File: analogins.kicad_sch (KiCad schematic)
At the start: 13 parts, among them J11 Conn_01x04_Socket, U12 MCP6042

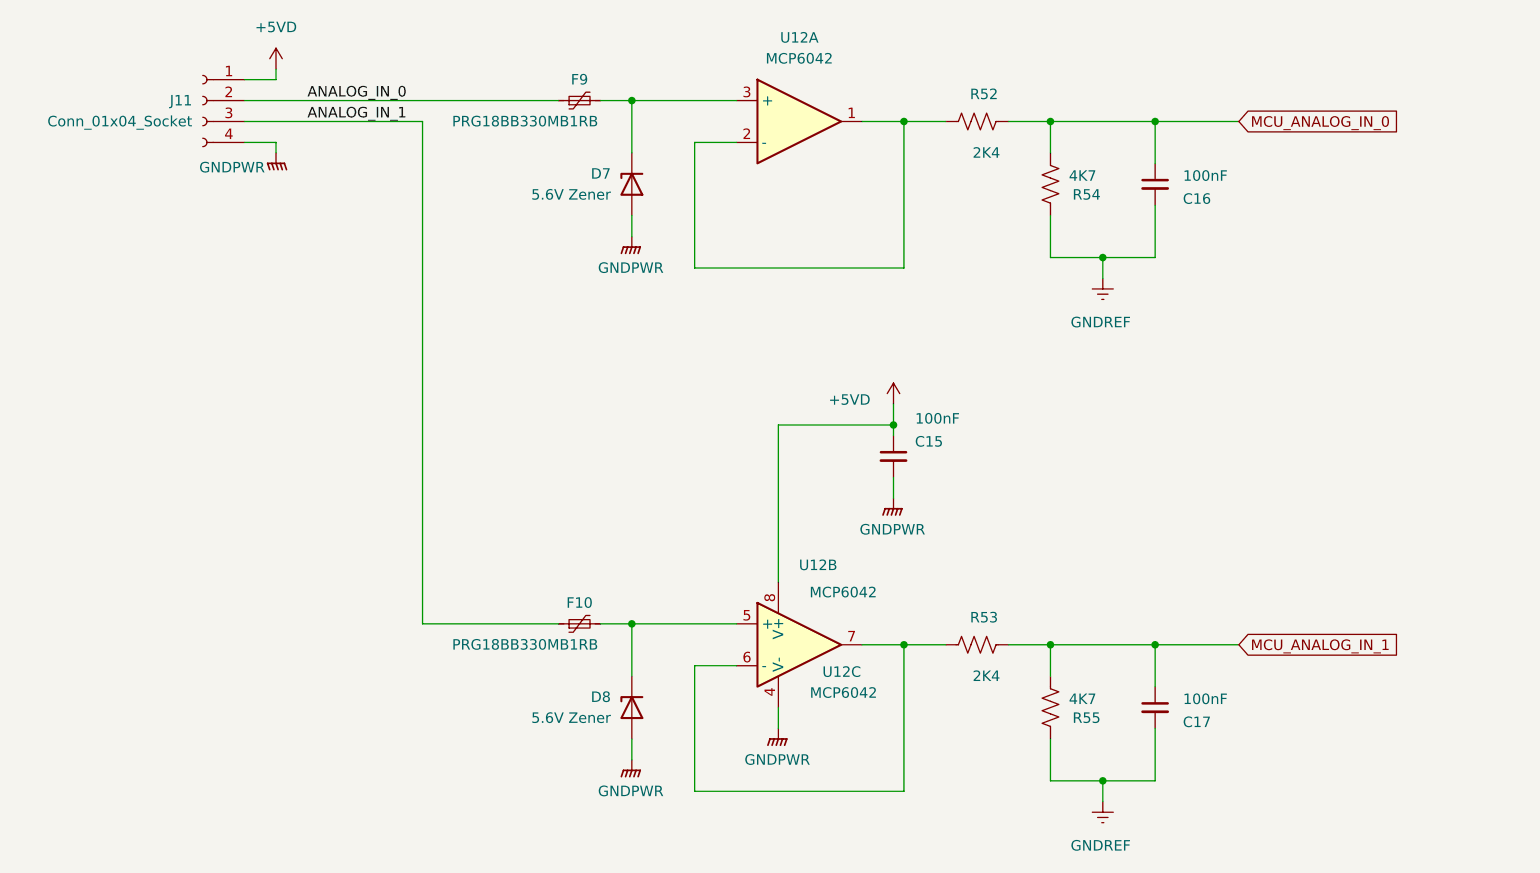
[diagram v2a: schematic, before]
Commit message: Added 3d Models for new terminal connectors for easy board verification before committing to build
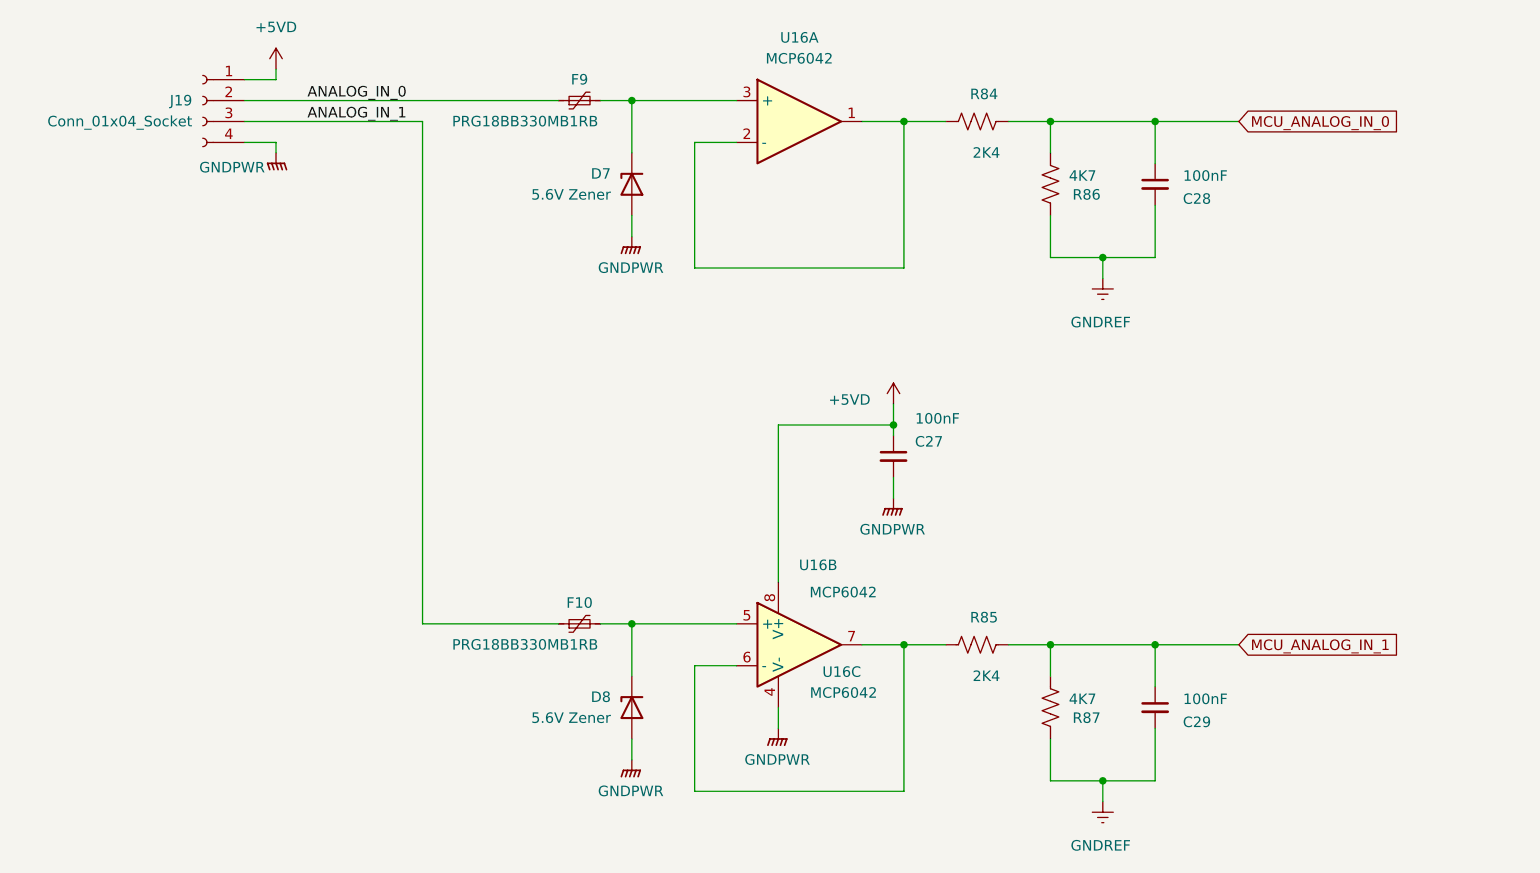
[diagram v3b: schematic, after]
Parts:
- renumbered C15 to C27, C16 to C28, C17 to C29, J11 to J19, R52 to R84, R53 to R85, R54 to R86, R55 to R87, U12 to U16
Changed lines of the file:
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@@
 		(on_board yes)
 		(dnp no)
-		(property "Reference" "#PWR0135"
+		(property "Reference" "#PWR0203"
 			(at 151.13 86.36 0)
 			(effects
@@
 			(project "Remora Nucleo F446ZE Hat"
 				(path "/5473abc6-7b93-43cc-a401-f691c4d7d7cf/c4dfed52-cba5-44a6-a641-6a90c0b6c0aa"
-					(reference "#PWR0135")
+					(reference "#PWR0203")
 					(unit 1)
 				)
@@
 		(on_board yes)
 		(dnp no)
-		(property "Reference" "R52"
+		(property "Reference" "R84"
 			(at 163.83 44.958 90)
 			(effects
@@
 			(project "Remora Nucleo F446ZE Hat"
 				(path "/5473abc6-7b93-43cc-a401-f691c4d7d7cf/c4dfed52-cba5-44a6-a641-6a90c0b6c0aa"
-					(reference "R52")
+					(reference "R84")
 					(unit 1)
 				)
@@
 		(on_board yes)
 		(dnp no)
-		(property "Reference" "U12"
+		(property "Reference" "U16"
 			(at 142.494 115.062 0)
 			(effects
@@
 			(project ""
 				(path "/5473abc6-7b93-43cc-a401-f691c4d7d7cf/c4dfed52-cba5-44a6-a641-6a90c0b6c0aa"
-					(reference "U12")
+					(reference "U16")
 					(unit 3)
 				)
@@
 		(on_board yes)
 		(dnp no)
-		(property "Reference" "C15"
+		(property "Reference" "C27"
 			(at 155.448 87.122 0)
 			(effects
@@
 			(project "Remora Nucleo F446ZE Hat"
 				(path "/5473abc6-7b93-43cc-a401-f691c4d7d7cf/c4dfed52-cba5-44a6-a641-6a90c0b6c0aa"
-					(reference "C15")
+					(reference "C27")
 					(unit 1)
 				)
@@
 		(on_board yes)
 		(dnp no)
-		(property "Reference" "R55"
+		(property "Reference" "R87"
 			(at 176.276 120.65 0)
 			(effects
@@
 			(project "Remora Nucleo F446ZE Hat"
 				(path "/5473abc6-7b93-43cc-a401-f691c4d7d7cf/c4dfed52-cba5-44a6-a641-6a90c0b6c0aa"
-					(reference "R55")
+					(reference "R87")
 					(unit 1)
 				)
@@
 		(dnp no)
 		(fields_autoplaced yes)
-		(property "Reference" "#PWR0132"
+		(property "Reference" "#PWR0200"
 			(at 119.38 67.31 0)
 			(effects
@@
 			(project "Remora Nucleo F446ZE Hat"
 				(path "/5473abc6-7b93-43cc-a401-f691c4d7d7cf/c4dfed52-cba5-44a6-a641-6a90c0b6c0aa"
-					(reference "#PWR0132")
+					(reference "#PWR0200")
 					(unit 1)
 				)
@@
 		(dnp no)
 		(fields_autoplaced yes)
-		(property "Reference" "#PWR0133"
+		(property "Reference" "#PWR0201"
 			(at 119.38 130.81 0)
 			(effects
@@
 			(project "Remora Nucleo F446ZE Hat"
 				(path "/5473abc6-7b93-43cc-a401-f691c4d7d7cf/c4dfed52-cba5-44a6-a641-6a90c0b6c0aa"
-					(reference "#PWR0133")
+					(reference "#PWR0201")
 					(unit 1)
 				)
@@
 		(dnp no)
 		(fields_autoplaced yes)
-		(property "Reference" "#PWR0134"
+		(property "Reference" "#PWR0202"
 			(at 137.16 127 0)
 			(effects
@@
 			(project "Remora Nucleo F446ZE Hat"
 				(path "/5473abc6-7b93-43cc-a401-f691c4d7d7cf/c4dfed52-cba5-44a6-a641-6a90c0b6c0aa"
-					(reference "#PWR0134")
+					(reference "#PWR0202")
 					(unit 1)
 				)
@@
 		(on_board yes)
 		(dnp no)
-		(property "Reference" "C16"
+		(property "Reference" "C28"
 			(at 187.96 57.658 0)
 			(effects
@@
 			(project "Remora Nucleo F446ZE Hat"
 				(path "/5473abc6-7b93-43cc-a401-f691c4d7d7cf/c4dfed52-cba5-44a6-a641-6a90c0b6c0aa"
-					(reference "C16")
+					(reference "C28")
 					(unit 1)
 				)
@@
 		(on_board yes)
 		(dnp no)
-		(property "Reference" "U12"
+		(property "Reference" "U16"
 			(at 141.986 102.108 0)
 			(effects
@@
 			(project ""
 				(path "/5473abc6-7b93-43cc-a401-f691c4d7d7cf/c4dfed52-cba5-44a6-a641-6a90c0b6c0aa"
-					(reference "U12")
+					(reference "U16")
 					(unit 2)
 				)
@@
 		(dnp no)
 		(fields_autoplaced yes)
-		(property "Reference" "J11"
+		(property "Reference" "J19"
 			(at 66.04 45.7199 0)
 			(effects
@@
 			(project "Remora Nucleo F446ZE Hat"
 				(path "/5473abc6-7b93-43cc-a401-f691c4d7d7cf/c4dfed52-cba5-44a6-a641-6a90c0b6c0aa"
-					(reference "J11")
+					(reference "J19")
 					(unit 1)
 				)
@@
 		(dnp no)
 		(fields_autoplaced yes)
-		(property "Reference" "U12"
+		(property "Reference" "U16"
 			(at 139.7 38.1 0)
 			(effects
@@
 			(project ""
 				(path "/5473abc6-7b93-43cc-a401-f691c4d7d7cf/c4dfed52-cba5-44a6-a641-6a90c0b6c0aa"
-					(reference "U12")
+					(reference "U16")
 					(unit 1)
 				)
@@
 		(on_board yes)
 		(dnp no)
-		(property "Reference" "C17"
+		(property "Reference" "C29"
 			(at 187.96 121.158 0)
 			(effects
@@
 			(project "Remora Nucleo F446ZE Hat"
 				(path "/5473abc6-7b93-43cc-a401-f691c4d7d7cf/c4dfed52-cba5-44a6-a641-6a90c0b6c0aa"
-					(reference "C17")
+					(reference "C29")
 					(unit 1)
 				)
@@
 		(on_board no)
 		(dnp no)
-		(property "Reference" "#PWR0138"
+		(property "Reference" "#PWR0206"
 			(at 176.53 137.16 0)
 			(effects
@@
 			(project "Remora Nucleo F446ZE Hat"
 				(path "/5473abc6-7b93-43cc-a401-f691c4d7d7cf/c4dfed52-cba5-44a6-a641-6a90c0b6c0aa"
-					(reference "#PWR0138")
+					(reference "#PWR0206")
 					(unit 1)
 				)
@@
 		(dnp no)
 		(fields_autoplaced yes)
-		(property "Reference" "#PWR0136"
+		(property "Reference" "#PWR0204"
 			(at 151.13 99.06 0)
 			(effects
@@
 			(project "Remora Nucleo F446ZE Hat"
 				(path "/5473abc6-7b93-43cc-a401-f691c4d7d7cf/c4dfed52-cba5-44a6-a641-6a90c0b6c0aa"
-					(reference "#PWR0136")
+					(reference "#PWR0204")
 					(unit 1)
 				)
@@
 		(on_board yes)
 		(dnp no)
-		(property "Reference" "R54"
+		(property "Reference" "R86"
 			(at 176.276 57.15 0)
 			(effects
@@
 			(project "Remora Nucleo F446ZE Hat"
 				(path "/5473abc6-7b93-43cc-a401-f691c4d7d7cf/c4dfed52-cba5-44a6-a641-6a90c0b6c0aa"
-					(reference "R54")
+					(reference "R86")
 					(unit 1)
 				)
@@
 		(dnp no)
 		(fields_autoplaced yes)
-		(property "Reference" "#PWR0130"
+		(property "Reference" "#PWR0198"
 			(at 76.2 45.72 0)
 			(effects
@@
 			(project "Remora Nucleo F446ZE Hat"
 				(path "/5473abc6-7b93-43cc-a401-f691c4d7d7cf/c4dfed52-cba5-44a6-a641-6a90c0b6c0aa"
-					(reference "#PWR0130")
+					(reference "#PWR0198")
 					(unit 1)
 				)
@@
 		(on_board no)
 		(dnp no)
-		(property "Reference" "#PWR0137"
+		(property "Reference" "#PWR0205"
 			(at 176.53 73.66 0)
 			(effects
@@
 			(project "Remora Nucleo F446ZE Hat"
 				(path "/5473abc6-7b93-43cc-a401-f691c4d7d7cf/c4dfed52-cba5-44a6-a641-6a90c0b6c0aa"
-					(reference "#PWR0137")
+					(reference "#PWR0205")
 					(unit 1)
 				)
@@
 		(on_board no)
 		(dnp no)
-		(property "Reference" "#PWR0131"
+		(property "Reference" "#PWR0199"
 			(at 76.2 57.15 0)
 			(effects
@@
 			(project "Remora Nucleo F446ZE Hat"
 				(path "/5473abc6-7b93-43cc-a401-f691c4d7d7cf/c4dfed52-cba5-44a6-a641-6a90c0b6c0aa"
-					(reference "#PWR0131")
+					(reference "#PWR0199")
 					(unit 1)
 				)
@@
 		(on_board yes)
 		(dnp no)
-		(property "Reference" "R53"
+		(property "Reference" "R85"
 			(at 163.83 108.458 90)
 			(effects
@@
 			(project "Remora Nucleo F446ZE Hat"
 				(path "/5473abc6-7b93-43cc-a401-f691c4d7d7cf/c4dfed52-cba5-44a6-a641-6a90c0b6c0aa"
-					(reference "R53")
-					(unit 1)
-				)
+					(reference "R85")
+					(unit 1)
+				)

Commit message: Caught some errors with spacing of jumpers, did some BOM consolidation and included BOM. Updates to Gerbers to reflect new changes.
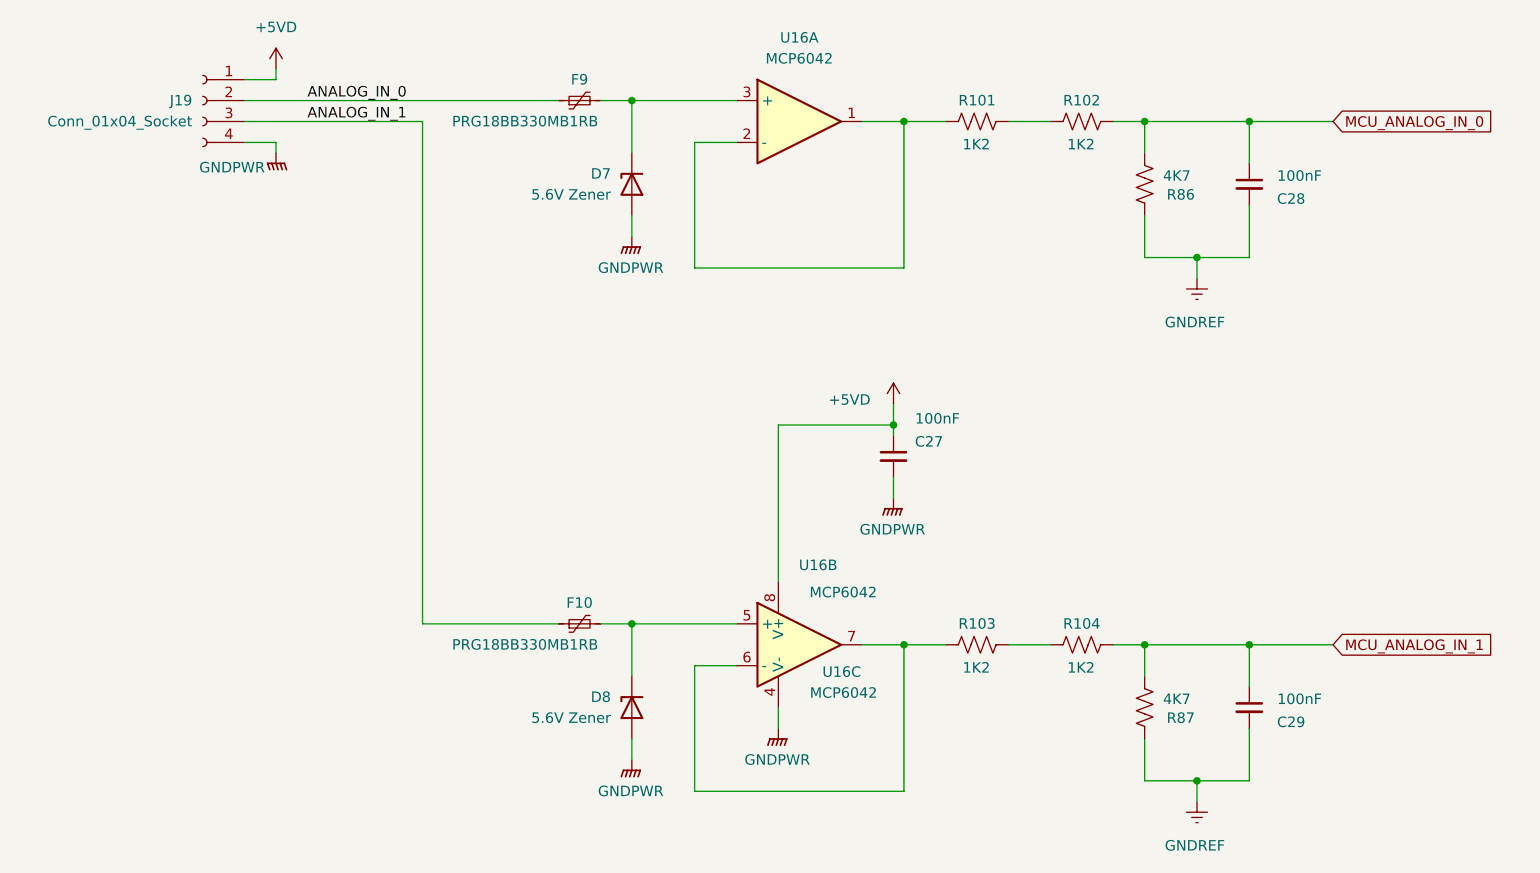
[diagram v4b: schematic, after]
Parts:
- removed R84, R85: 2K4, Resistor_SMD:R_1206_3216Metric_Pad1.30x1.75mm_HandSolder, symbol Device:R_US
- added R101, R102, R103, R104: 1K2, Resistor_SMD:R_1206_3216Metric_Pad1.30x1.75mm_HandSolder, symbol Device:R_US
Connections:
- net MCU_ANALOG_IN_0: now also R102.1
- net MCU_ANALOG_IN_1: now also R104.1
- net at U16.1, U16.2 (-): now also R101.2
- net at U16.6 (-), U16.7: now also R103.2
- new net: R101.1, R102.2
- new net: R103.1, R104.2
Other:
- moved on the sheet: C28, C29, R86, R87

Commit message: Some file changes and output new gerbers + BOM and centroid file for PCBWay Order
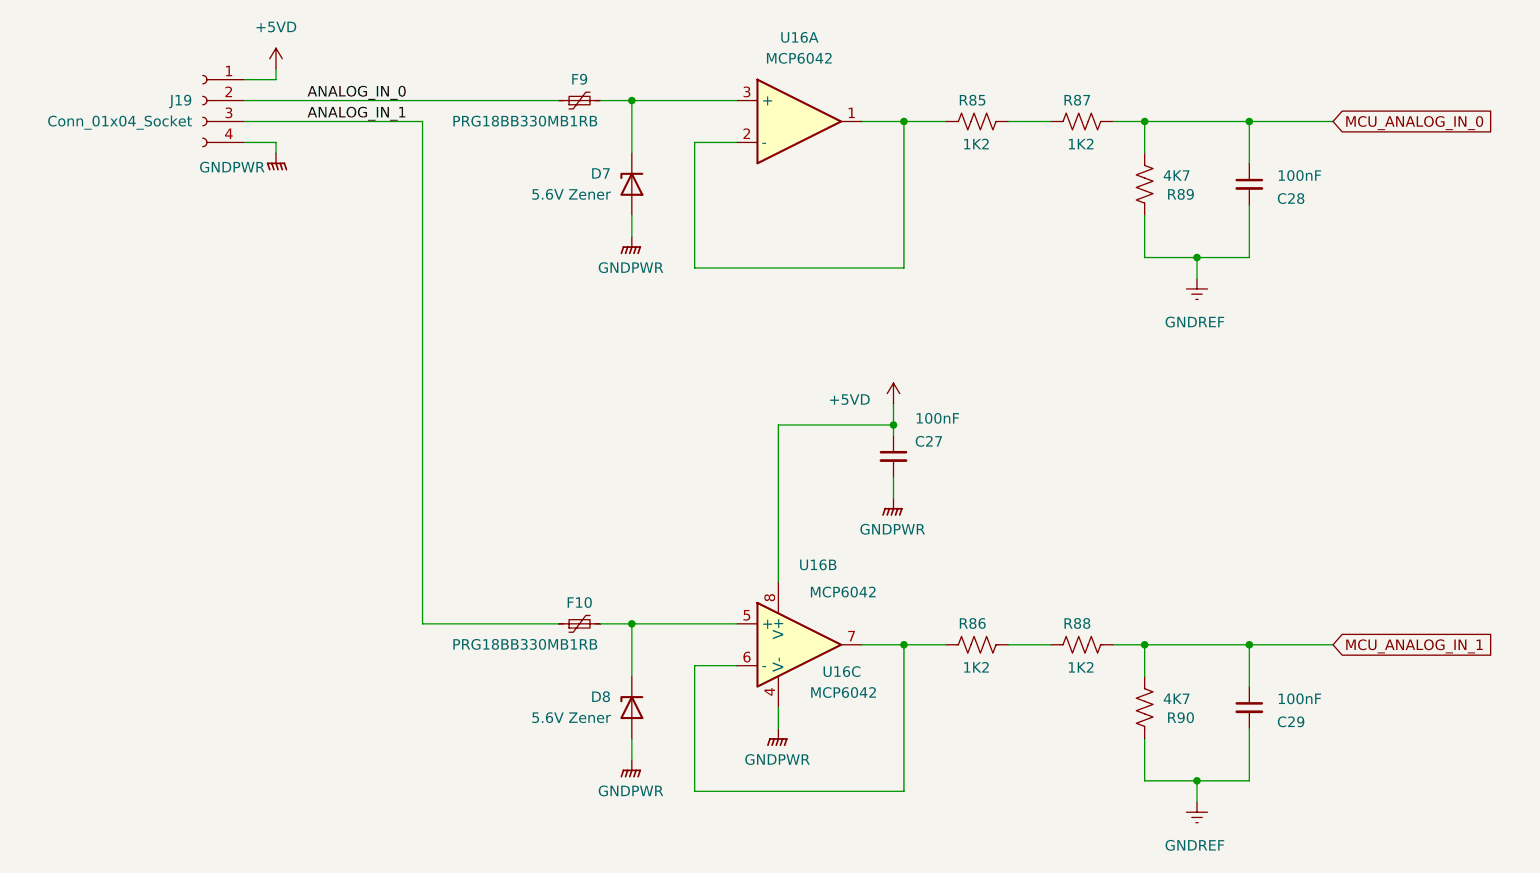
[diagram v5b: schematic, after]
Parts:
- renumbered R101 to R85, R103 to R86, R102 to R87, R104 to R88, R86 to R89, R87 to R90
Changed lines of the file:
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@@
 		(on_board yes)
 		(dnp no)
-		(property "Reference" "R101"
+		(property "Reference" "R85"
 			(at 159.004 45.72 90)
 			(effects
@@
 			(project "Remora Nucleo F446ZE Hat"
 				(path "/5473abc6-7b93-43cc-a401-f691c4d7d7cf/c4dfed52-cba5-44a6-a641-6a90c0b6c0aa"
-					(reference "R101")
+					(reference "R85")
 					(unit 1)
 				)
@@
 		(on_board yes)
 		(dnp no)
-		(property "Reference" "R102"
+		(property "Reference" "R87"
 			(at 171.704 45.72 90)
 			(effects
@@
 			(project "Remora Nucleo F446ZE Hat"
 				(path "/5473abc6-7b93-43cc-a401-f691c4d7d7cf/c4dfed52-cba5-44a6-a641-6a90c0b6c0aa"
-					(reference "R102")
+					(reference "R87")
 					(unit 1)
 				)
@@
 		(on_board yes)
 		(dnp no)
-		(property "Reference" "R87"
+		(property "Reference" "R90"
 			(at 187.706 120.65 0)
 			(effects
@@
 			(project "Remora Nucleo F446ZE Hat"
 				(path "/5473abc6-7b93-43cc-a401-f691c4d7d7cf/c4dfed52-cba5-44a6-a641-6a90c0b6c0aa"
-					(reference "R87")
+					(reference "R90")
 					(unit 1)
 				)
@@
 		(on_board yes)
 		(dnp no)
-		(property "Reference" "R103"
+		(property "Reference" "R86"
 			(at 159.004 109.22 90)
 			(effects
@@
 			(project "Remora Nucleo F446ZE Hat"
 				(path "/5473abc6-7b93-43cc-a401-f691c4d7d7cf/c4dfed52-cba5-44a6-a641-6a90c0b6c0aa"
-					(reference "R103")
+					(reference "R86")
 					(unit 1)
 				)
@@
 		(on_board yes)
 		(dnp no)
-		(property "Reference" "R104"
+		(property "Reference" "R88"
 			(at 171.704 109.22 90)
 			(effects
@@
 			(project "Remora Nucleo F446ZE Hat"
 				(path "/5473abc6-7b93-43cc-a401-f691c4d7d7cf/c4dfed52-cba5-44a6-a641-6a90c0b6c0aa"
-					(reference "R104")
+					(reference "R88")
 					(unit 1)
 				)
@@
 		(on_board yes)
 		(dnp no)
-		(property "Reference" "R86"
+		(property "Reference" "R89"
 			(at 187.706 57.15 0)
 			(effects
@@
 			(project "Remora Nucleo F446ZE Hat"
 				(path "/5473abc6-7b93-43cc-a401-f691c4d7d7cf/c4dfed52-cba5-44a6-a641-6a90c0b6c0aa"
-					(reference "R86")
-					(unit 1)
-				)
+					(reference "R89")
+					(unit 1)
+				)

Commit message: Fixed error in opamp part number
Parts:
- U16: Digikey Part Number 150-MCP6042T-E/MSVAOCT-ND -> MCP6042-I/SN-ND; Digikey URL https://www.digikey.com/en/products/detail/microchip-technology/mcp6042t-e-snvao/9993094 -> https://www.digikey.com/en/products/detail/microchip-technology/MCP6042-I-SN/413367
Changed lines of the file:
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@@
 			)
 		)
-		(property "Digikey Part Number" "150-MCP6042T-E/MSVAOCT-ND"
+		(property "Digikey Part Number" "MCP6042-I/SN-ND"
 			(at 139.7 111.76 0)
 			(effects
@@
 			)
 		)
-		(property "Digikey URL" "https://www.digikey.com/en/products/detail/microchip-technology/mcp6042t-e-snvao/9993094"
+		(property "Digikey URL" "https://www.digikey.com/en/products/detail/microchip-technology/MCP6042-I-SN/413367"
 			(at 139.7 111.76 0)
 			(effects
@@
 			)
 		)
-		(property "Digikey Part Number" "150-MCP6042T-E/MSVAOCT-ND"
+		(property "Digikey Part Number" "MCP6042-I/SN-ND"
 			(at 139.7 111.76 0)
 			(effects
@@
 			)
 		)
-		(property "Digikey URL" "https://www.digikey.com/en/products/detail/microchip-technology/mcp6042t-e-snvao/9993094"
+		(property "Digikey URL" "https://www.digikey.com/en/products/detail/microchip-technology/MCP6042-I-SN/413367"
 			(at 139.7 111.76 0)
 			(effects
@@
 			)
 		)
-		(property "Digikey Part Number" "150-MCP6042T-E/MSVAOCT-ND"
+		(property "Digikey Part Number" "MCP6042-I/SN-ND"
 			(at 139.7 48.26 0)
 			(effects
@@
 			)
 		)
-		(property "Digikey URL" "https://www.digikey.com/en/products/detail/microchip-technology/mcp6042t-e-snvao/9993094"
+		(property "Digikey URL" "https://www.digikey.com/en/products/detail/microchip-technology/MCP6042-I-SN/413367"
 			(at 139.7 48.26 0)
 			(effects
